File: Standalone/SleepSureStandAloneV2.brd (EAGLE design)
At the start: 62.3 x 37 mm, 66 parts, among them IC1 CP2104, Q1 mmbt2222, Q2 mmbt2222, Q3 DMG3415U, SW2 KMR2, U1 ADS1299-4PAG, U2 AP2112-3.3, U3 MCP73831T-2ACI/OT, X1 JSTPH, X2 ESP32_WROOM32_SKINNY, X4 20329

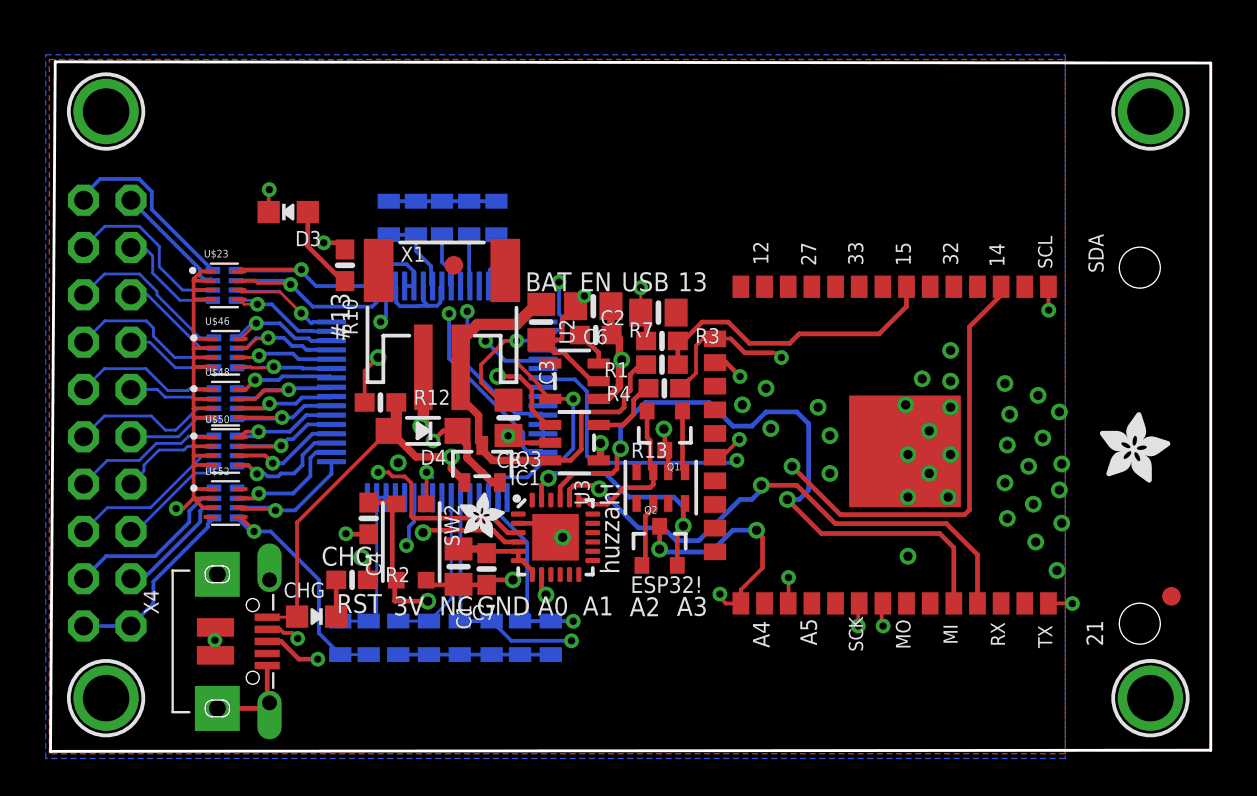
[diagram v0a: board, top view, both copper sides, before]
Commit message: Added power booster to standalone board
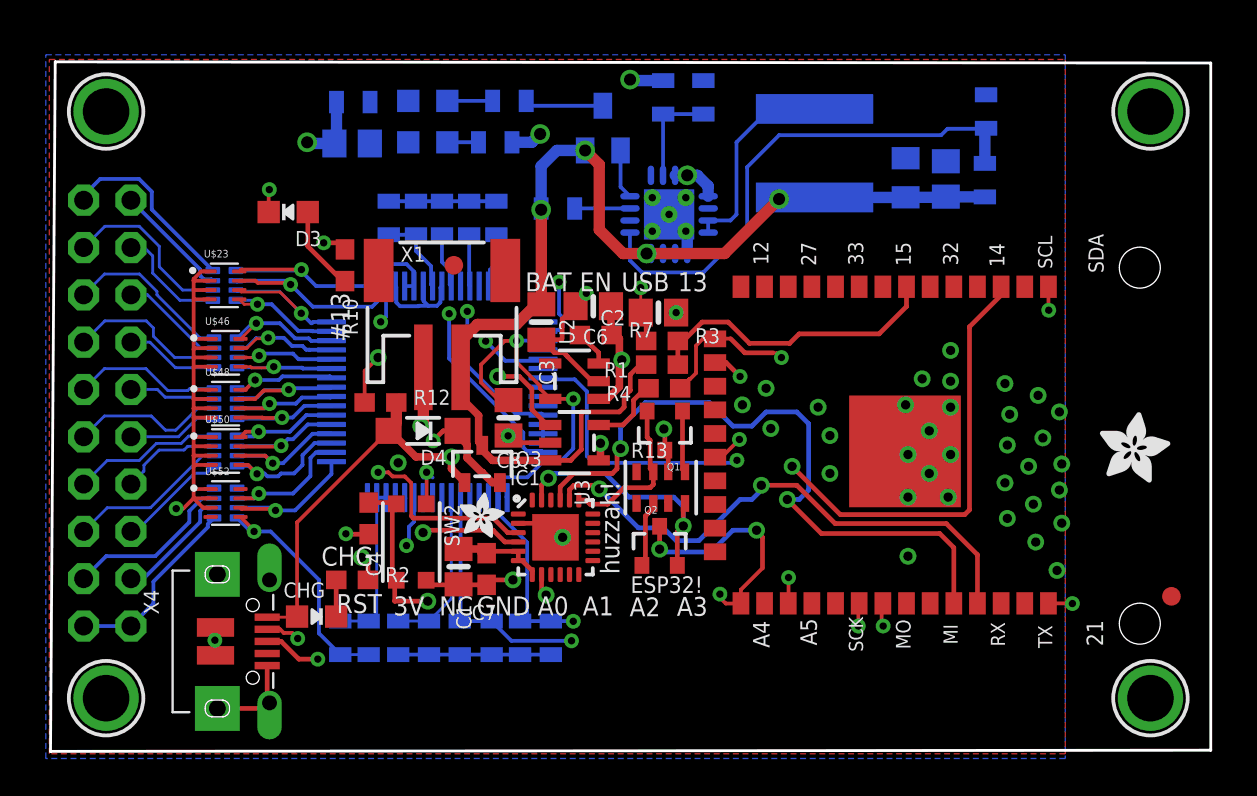
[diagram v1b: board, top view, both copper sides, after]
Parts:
- added C17: 10uF, microbuilder:0805-NO
- added C18: 2.2uF, microbuilder:0805-NO
- added C19: 0.1uF, microbuilder:0805_10MGAP
- added C22: 100uF, SparkFun-Capacitors:0805
- added LED1: RED, microbuilder:CHIPLED_0805_NOOUTLINE
- added LED2: BLUE, microbuilder:CHIPLED_0805_NOOUTLINE
- added R11, R9: 1k, SparkFun-Resistors:0805
- added R16: 1.87M, SparkFun-Resistors:0805
- added R17: 340k, SparkFun-Resistors:0805
- added R18: 1.8M, SparkFun-Resistors:0805
- added R19, R5: 200k, SparkFun-Resistors:0805
- added T1: MMUN2133LT1G, transistor:SC59-BEC
- added U$55: 6.8uH, ADS_Feather:0628
- added U4: TPS61090RSAR, microbuilder:PVQFN-16
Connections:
- new net ENABLE: R5.1, U4.11
- new net LBO: T1.B, U4.12
- new net N$16: U$55.P$2, U4.3, U4.4
- new net N$17: R16.1, R17.2, U4.9
- new net N$18: R18.1, R19.2, U4.14
- new net N$19: LED2.A, R9.1
- new net N$20: LED1.A, R11.1
- new net N$21: R11.2, T1.C
- net 5V: now also C18.1, C22.1, R18.2, R9.2, U4.1, U4.15, U4.16
- net GND: now also C17.2, C18.2, C19.2, C22.2, LED1.C, LED2.C, R17.1, R19.1, U4.10, U4.13, U4.5, U4.6, U4.7, U4.P$18, U4.P$19, U4.P$20, U4.P$21, U4.P$22, U4.THERMAL
- net VBAT: now also C17.1, C19.1, R16.2, R5.2, T1.E, U$55.P$1, U4.8
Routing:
- net VBAT: track 25.0 -> 62.2 mm, vias 0 -> 4
- net N$17: track 0.00 -> 27.9 mm
- net N$16: track 0.00 -> 11.1 mm
- net 5V: track 21.9 -> 31.7 mm, vias 3 -> 7
- net 3.3V: track 37.4 -> 45.7 mm, vias 3 -> 4
- net N$18: track 0.00 -> 5.45 mm
- net N$21: track 0.00 -> 4.22 mm
- net GND: track 99.4 -> 103.4 mm
- net ENABLE: track 0.00 -> 2.97 mm
- net LBO: track 0.00 -> 2.68 mm
- net N$20: track 0.00 -> 2.43 mm
- net N$19: track 0.00 -> 1.67 mm

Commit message: changed usb header'
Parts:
- removed X4: 20329, microbuilder:4UCONN_20329_V2
- added J1: 10118192-0002LF, ADS_Feather:AMPHENOL_10118192-0002LF
- added U$62, U$66: (no value), ADS_Feather:SOD123FL
- moved LED2 3.05 mm to (20.8, 35.7)
- moved R9 3.05 mm to (24.4, 35.7)
- moved R19 2.90 mm to (32.6, 34.3)
- moved CHG 2.74 mm to (12.7, 9.14)
- moved LED1 2.53 mm to (20.1, 32.4)
- moved R11 2.53 mm to (24.4, 32.4)
- moved R18 2.23 mm to (35.3, 34.3)
- moved C18 0.74 mm to (16.3, 31.9), turned to 270 degrees
- moved C22 0.60 mm to (16.3, 35.3), turned to 90 degrees
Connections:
- removed net N$2: IC1.3, X4.D+
- removed net N$6: IC1.4, X4.D-
- new net 5VBAT: C18.1, C22.1, R18.2, R9.2, U$66.A, U4.1, U4.15, U4.16
- new net D+: IC1.3, J1.3
- new net D-: IC1.4, J1.2
- net 5V: now also U$62.C, U$66.C; no longer C18.1, C22.1, R18.2, R9.2, U4.1, U4.15, U4.16
- net GND: now also J1.5; no longer X4.BASE@1, X4.BASE@2, X4.GND, X4.SPRT@1, X4.SPRT@2, X4.SPRT@3, X4.SPRT@4
- net VBUS: now also J1.1, U$62.A; no longer X4.VBUS
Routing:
- net 5VBAT: track 0.00 -> 33.5 mm
- net N$6: track 24.6 -> 0.00 mm, vias 3 -> 0
- net N$2: track 24.4 -> 0.00 mm, vias 2 -> 0
- net D-: track 0.00 -> 19.1 mm, vias 0 -> 2
- net D+: track 0.00 -> 18.0 mm, vias 0 -> 2
- net 5V: track 31.7 -> 27.4 mm, vias 7 -> 5
- net GND: track 103.4 -> 101.2 mm, vias 47 -> 48
- net N$21: track 4.22 -> 5.54 mm
- net VBUS: track 42.9 -> 44.1 mm, vias 3 -> 2
- net N$18: track 5.45 -> 6.13 mm

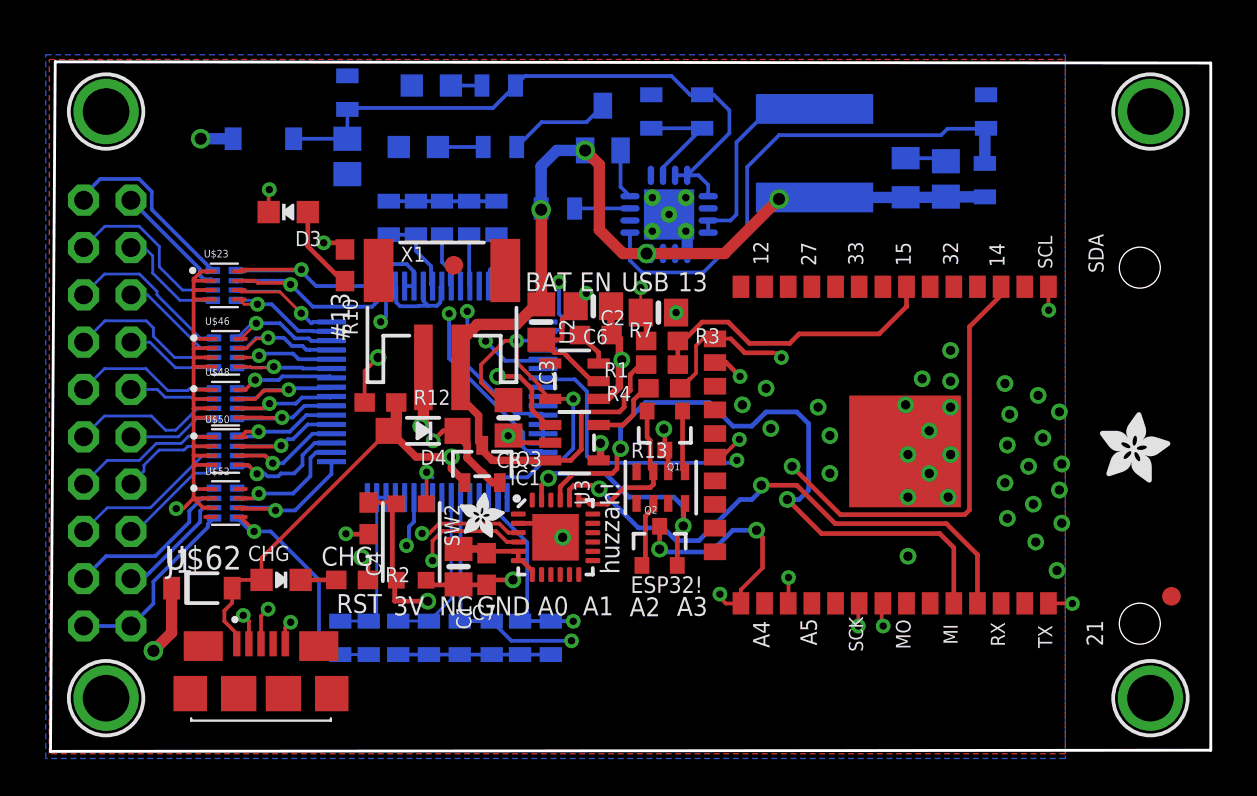
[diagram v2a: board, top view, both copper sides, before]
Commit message: modified design file and removed errors
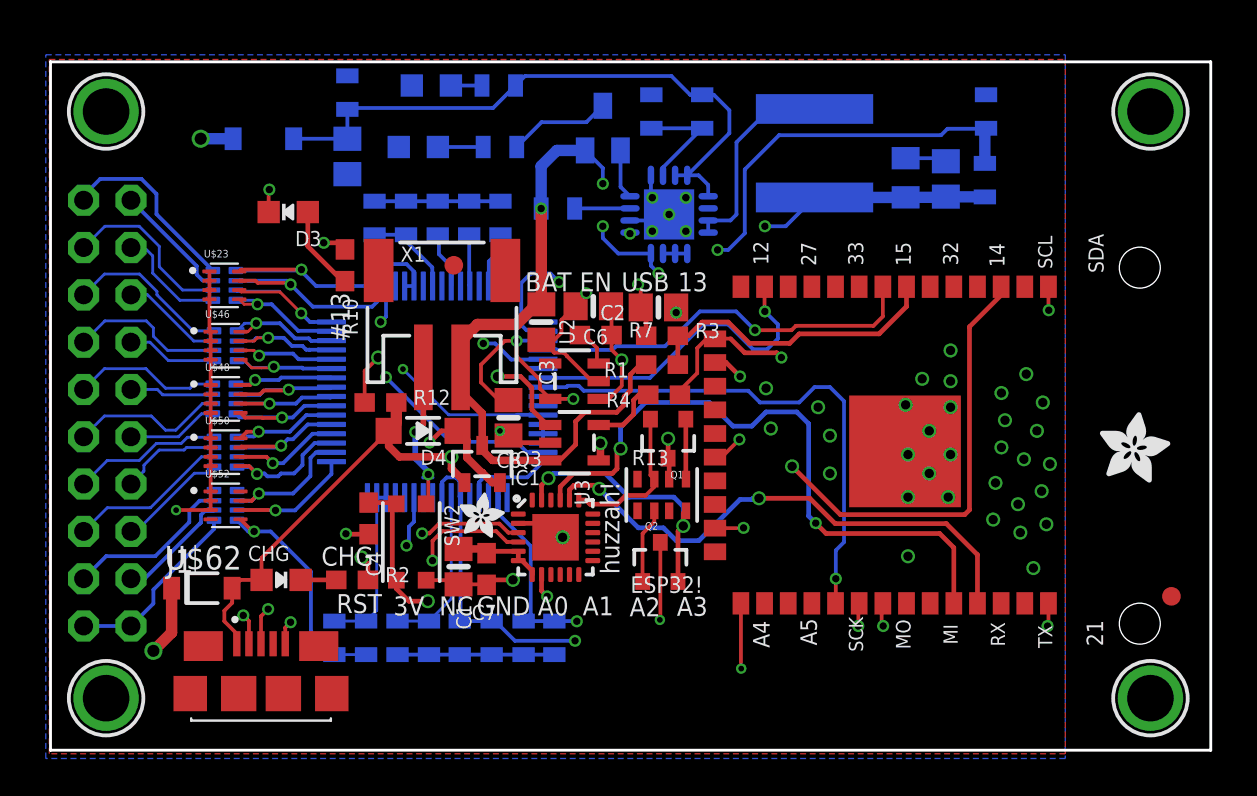
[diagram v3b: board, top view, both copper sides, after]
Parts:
- removed U$13: (no value), microbuilder:PCBFEAT-REV-040
- removed U$43: (no value), silks:HUZZAH32
- removed U$7: (no value), microbuilder:ADAFRUIT_5MM
- removed U$9: (no value), silks:FEATHERLOGO_MED
- U$23, U$46, U$48, U$50, U$52: value W2A45C103MAT2A -> 1nF
- U$44, U$45, U$47, U$49, U$51: value (none) -> 2.2k
- U$62, U$66: value (none) -> MRB120
- moved Q2 0.86 mm to (33.1, 10.1)
- moved C13 0.76 mm to (17.7, 28.6)
- moved C10 0.53 mm to (19.4, 28.6)
- moved Q1 0.47 mm to (33.5, 16.8)
- moved R13 0.40 mm to (33.1, 13.7)
- moved U$45 0.38 mm to (9.72, 21.7)
- moved U$46 0.38 mm to (9.72, 21.7)
- moved R4 0.34 mm to (33.3, 19.1)
- moved C25 0.32 mm to (15.6, 6.03)
- moved C2 0.28 mm to (33.0, 23.8)
- moved R3 0.28 mm to (33.1, 22.3)
- moved U$47 0.26 mm to (9.65, 18.9)
- moved U$48 0.25 mm to (9.72, 18.9)
- moved C9 0.23 mm to (21.1, 28.6)
- moved C24 0.22 mm to (24.5, 28.6)
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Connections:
- removed net IO14_A6: X2.13
- removed net IO15_A8: X2.23
- removed net IO32_A7: X2.8
- removed net SCLK: U1.40
- new net GPIO0: Q2.3, X2.25
- new net IO16: X2.27
- net ADS_CS: now also X2.13; no longer Q2.3, X2.25
- net ADS_RESET: now also X2.8
- net DRDY: now also X2.23; no longer X2.27
- net SCK: now also U1.40
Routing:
- net SCK: track 0.00 -> 28.3 mm, vias 0 -> 1
- net ADS_RESET: track 0.00 -> 21.4 mm, vias 0 -> 1
- net ADS_CS: track 35.5 -> 17.7 mm, vias 4 -> 1
- net GND: track 101.2 -> 85.7 mm, vias 48 -> 47
- net GPIO0: track 0.00 -> 13.1 mm, vias 0 -> 2
- net 3.3V: track 45.7 -> 41.5 mm
- net 5V: track 27.4 -> 30.4 mm
- net VBAT: track 62.2 -> 64.9 mm, vias 4 -> 5
- net MOSI: track 35.2 -> 37.5 mm
- net N$17: track 27.9 -> 26.1 mm, vias 0 -> 2
- net DRDY: track 41.7 -> 43.4 mm
- net VBUS: track 44.1 -> 45.8 mm, vias 2 -> 3
- net MISO: track 42.3 -> 44.0 mm
- net RXD0: track 36.1 -> 34.7 mm
- net RESET: track 68.4 -> 67.2 mm
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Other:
- outline, holes or cut-outs redrawn
- board text removed: "12/A11"
- board text removed: "13/A12"
- board text removed: "14/A6"
- board text removed: "15/A8"
- board text removed: "27/A10"
- board text removed: "32/A7"
- board text removed: "33/A9"
- board text removed: "A0 DAC2"
- board text removed: "A1 DAC1"
- board text removed: "A2/34"
- board text removed: "A3/39"
- board text removed: "A4/36"
- board text removed: "A5/4"
- board text removed: "Contains FCCID 2AC7Z-ESP32"
- board text removed: "En"
- board text removed: "MISO/19"
- board text removed: "MOSI/18"
- board text removed: "RX/16"
- board text removed: "SCK/5"
- board text removed: "SCL/22"
- board text removed: "SDA/23"
- board text removed: "TX/17"

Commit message: changed footprint of 100uF caps to 1206
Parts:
- removed C20: 100uF, SparkFun-Capacitors:0805
- removed U$35: FIDUCIAL_1MM, microbuilder:FIDUCIAL_1MM
- added C21: 0.1uF, SparkFun-Capacitors:0805
- C19: value 0.1uF -> 100uF; device microbuilder:0805_10MGAP -> SparkFun-Capacitors:1206
- C22: device SparkFun-Capacitors:0805 -> SparkFun-Capacitors:1206
- moved C19 32.1 mm to (14.5, 35.5), turned to 0 degrees
- moved C22 9.17 mm to (23.1, 29.2)
- moved C18 0.78 mm to (15.8, 31.2)
- moved C24 0.66 mm to (25.1, 28.6)
- moved LED1 0.18 mm to (20.1, 32.6)
- moved R11 0.15 mm to (24.4, 32.5)
- moved C10 0.10 mm to (19.3, 28.6)
- moved C13 0.10 mm to (17.6, 28.6)
- moved C9 0.10 mm to (21.0, 28.6)
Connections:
- net 5VBAT: now also C19.1; no longer C22.1
- net GND: now also C21.2; no longer C20.2
- net N$9: now also C22.1; no longer C20.1
- net VBAT: now also C21.1; no longer C19.1
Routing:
- net GND: track 85.7 -> 81.5 mm, vias 47 -> 48
- net 5VBAT: track 33.5 -> 36.4 mm
- net VBAT: track 64.9 -> 63.1 mm

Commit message: added START pin of ADS1299 to gpio27
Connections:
- removed net IO27_A10: X2.12
- new net ADS_START: U1.38, X2.12
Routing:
- net ADS_START: track 0.00 -> 25.6 mm, vias 0 -> 3
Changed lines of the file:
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@@
 <contactref element="X2" pad="9"/>
-</signal>
-<signal name="IO27_A10">
-<contactref element="X2" pad="12"/>
 </signal>
 <signal name="MISO">
@@
 <contactref element="X2" pad="27"/>
 </signal>
+<signal name="ADS_START">
+<contactref element="U1" pad="38"/>
+<contactref element="X2" pad="12"/>
+<via x="22.5634" y="23.4696" extent="1-16" drill="0.35"/>
+<wire x1="26.762" y1="20.4905" x2="24.8993" y2="20.4905" width="0.1524" layer="16"/>
+<wire x1="24.8993" y1="20.4905" x2="24.257" y2="21.1328" width="0.1524" layer="16"/>
+<wire x1="24.257" y1="21.1328" x2="23.2156" y2="21.1328" width="0.1524" layer="16"/>
+<wire x1="23.2156" y1="21.1328" x2="22.5634" y2="21.785" width="0.1524" layer="16"/>
+<wire x1="22.5634" y1="21.785" x2="22.5634" y2="23.4696" width="0.1524" layer="16"/>
+<via x="30.2006" y="25.7556" extent="1-16" drill="0.35"/>
+<wire x1="39.925" y1="24.883" x2="39.925" y2="25.05360625" width="0.1524" layer="1"/>
+<wire x1="39.925" y1="25.05360625" x2="38.76510625" y2="26.2135" width="0.1524" layer="1"/>
+<wire x1="30.2006" y1="25.7556" x2="30.1829" y2="25.7379" width="0.1524" layer="2"/>
+<wire x1="30.1829" y1="25.7379" x2="24.8317" y2="25.7379" width="0.1524" layer="2"/>
+<wire x1="24.8317" y1="25.7379" x2="22.5634" y2="23.4696" width="0.1524" layer="2"/>
+<via x="38.76510625" y="26.2135" extent="1-16" drill="0.35"/>
+<wire x1="32.24880625" y1="25.7556" x2="30.2006" y2="25.7556" width="0.1524" layer="15"/>
+<wire x1="32.70670625" y1="26.2135" x2="32.24880625" y2="25.7556" width="0.1524" layer="15"/>
+<wire x1="38.76510625" y1="26.2135" x2="32.70670625" y2="26.2135" width="0.1524" layer="15"/>
+</signal>
 </signals>

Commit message: Uploading final standalone and feather files
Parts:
- removed R13: 10K, microbuilder:RESPACK_4X0603
- removed U$14: (no value), microbuilder:ADAFRUIT_2.5MM
- removed U$15: (no value), microbuilder:ADAFRUIT_3.5MM
- removed U$34: FIDUCIAL_1MM, microbuilder:FIDUCIAL_1MM
- added U$7: 10k, SleepSureLib:RESCAXS50P200X100X45-8N
- JP2: value (none) -> 2x10
- U3: value MCP73831T-2ACI/OT -> LiPoly
- moved C1 1.02 mm to (22.3, 8.84)
- moved U$19 0.97 mm to (59.7, 35.2)
- moved U$6 0.92 mm to (3.30, 35.2)
- moved C7 0.36 mm to (24.0, 9.50)
- moved U$31 0.33 mm to (59.7, 2.79)
- renumbered X1 to 2PIN
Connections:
- removed net N$12: Q1.1, R13.5
- removed net N$13: Q2.1, R13.2
- new net N$2: Q2.1, U$7.1
- new net N$6: Q1.1, U$7.5
- net 3.3V: now also U$7.2; no longer R13.3
- net DTR: now also U$7.4; no longer R13.4
- net RESET: now also U$7.7; no longer R13.6
- net RTS: now also U$7.8; no longer R13.7
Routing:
- net N$2: track 0.00 -> 5.30 mm, vias 0 -> 2
- net N$13: track 4.06 -> 0.00 mm
- net N$6: track 0.00 -> 3.30 mm
- net N$12: track 3.23 -> 0.00 mm
- net GND: track 81.5 -> 82.7 mm
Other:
- board size 62.3 x 37 mm -> 63 x 38 mm
- board text added: "1SRB2"
- board text added: "BIAS"
- board text added: "Ian Romano Nate Joseph Kyle Sapia Matias Saavedra Silva"
- board text added: "P1N"
- board text added: "P2N"
- board text added: "P3N"
- board text added: "P4N"
- board text added: "P5N"
- board text added: "P6N"
- board text added: "P7N"
- board text added: "P8N"
- board text added: "SleepSure ADS1299 ESP32 12 Apr 2021 Rev 3"
- board text removed: "3.7/4.2V LiPoly Batt µUSB charge"
- board text removed: "3V"
- board text removed: "A0"
- board text removed: "A1"
- board text removed: "A2"
- board text removed: "A3"
- board text removed: "ESP32 Feather 16MB Flash WiFI+BT"
- board text removed: "ESP32!"
- board text removed: "GND"
- board text removed: "NC"
- board text removed: "RST"
